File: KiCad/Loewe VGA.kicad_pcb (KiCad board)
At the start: 2 copper layers, 54.5 x 33.2 mm, 29 parts, among them U1 74HCT86

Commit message: Add project title and link to PCB silkscreen.
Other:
- board text added: "Loewe TVs Q2500 VGA Module"
- board text added: "github.com/proboterror/Loewe_VGA_Module_Q2500"
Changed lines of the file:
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@@
 			(at 4.315 -2.58 -90)
 			(layer "F.SilkS")
+			(hide yes)
 			(effects
 				(font
@@
 			(unlocked yes)
 			(layer "B.SilkS")
+			(hide yes)
 			(effects
 				(font
@@
 		)
 	)
+	(gr_text "github.com/proboterror/Loewe_VGA_Module_Q2500"
+		(at 172.307074 98.5 0)
+		(layer "B.SilkS")
+		(effects
+			(font
+				(size 1 1)
+				(thickness 0.15)
+			)
+			(justify left bottom mirror)
+		)
+	)
 	(gr_text "VCC"
 		(at 131.5 94.3 0)
@@
 			)
 			(justify left bottom mirror)
+		)
+	)
+	(gr_text "Loewe TVs Q2500 VGA Module"
+		(at 170.1 96.750072 0)
+		(layer "B.SilkS")
+		(effects
+			(font
+				(size 1.5 1.5)
+				(thickness 0.2)
+			)
+			(justify left bottom mirror)

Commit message: Connect VGA pin 8 to GND.
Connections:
- W801 pad 8: unconnected-(W801-Pad8) -> GND
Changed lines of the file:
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@@
 	(net 25 "unconnected-(W801-Pad0)")
 	(net 26 "unconnected-(W801-Pad0)_0")
-	(net 27 "unconnected-(W801-Pad8)")
-	(net 28 "unconnected-(W801-Pad4)")
-	(net 29 "unconnected-(W801-Pad9)")
+	(net 27 "unconnected-(W801-Pad4)")
+	(net 28 "unconnected-(W801-Pad9)")
 	(footprint "Capacitor_SMD:C_0805_2012Metric_Pad1.18x1.45mm_HandSolder"
 		(layer "F.Cu")
@@
 			(layers "*.Cu" "*.Mask")
 			(remove_unused_layers no)
-			(net 28 "unconnected-(W801-Pad4)")
+			(net 27 "unconnected-(W801-Pad4)")
 			(pintype "passive+no_connect")
 		)
@@
 			(layers "*.Cu" "*.Mask")
 			(remove_unused_layers no)
-			(net 27 "unconnected-(W801-Pad8)")
-			(pintype "passive+no_connect")
+			(net 1 "GND")
+			(pintype "passive")
 		)
 		(pad "9" thru_hole circle
@@
 			(layers "*.Cu" "*.Mask")
 			(remove_unused_layers no)
-			(net 29 "unconnected-(W801-Pad9)")
+			(net 28 "unconnected-(W801-Pad9)")
 			(pintype "passive+no_connect")
 		)

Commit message: Replace custom 3225 footprint for L826, L816 with standard 1210(3225). Add 4.7uH value for L826, L816 to schematic (use value from Q2300 board).
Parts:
- L816, L826: value LL3225M -> 4u7; footprint Loewe VGA:L3225M -> Inductor_SMD:L_1210_3225Metric_Pad1.42x2.65mm_HandSolder

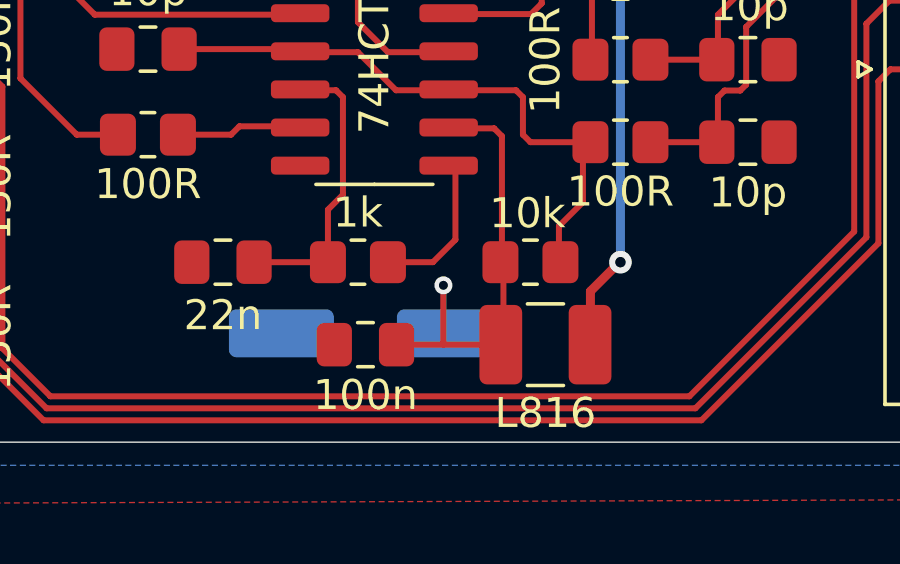
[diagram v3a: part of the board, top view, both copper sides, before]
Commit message: Add telegram channel link. Adjust power tracks width.
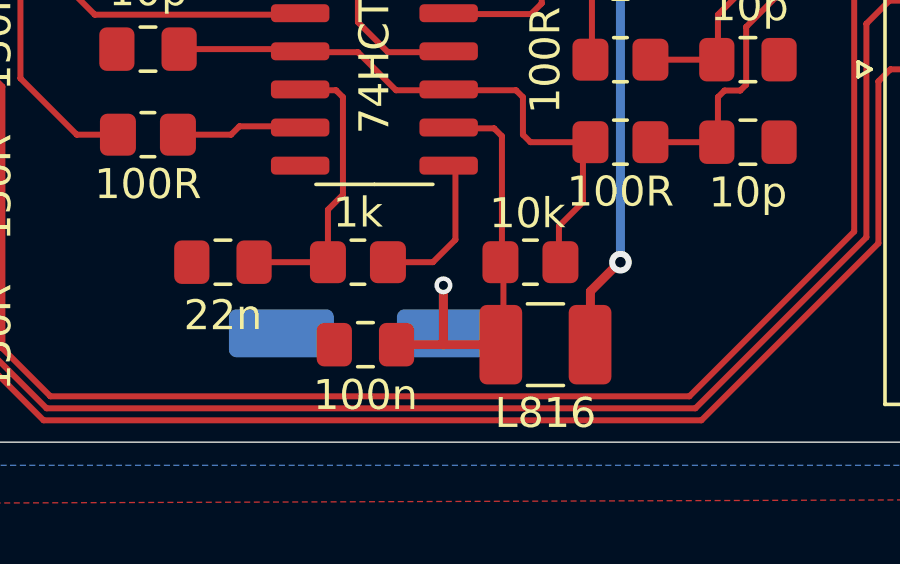
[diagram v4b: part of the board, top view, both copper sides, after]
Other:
- board text added: "github.com/proboterror/Loewe_VGA_Module_Q2500 t.me/dmg_crt"
- board text removed: "github.com/proboterror/Loewe_VGA_Module_Q2500"
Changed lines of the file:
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@@
 		)
 	)
-	(gr_text "github.com/proboterror/Loewe_VGA_Module_Q2500"
-		(at 172.307074 98.5 0)
-		(layer "B.SilkS")
-		(effects
-			(font
-				(size 1 1)
-				(thickness 0.15)
-			)
-			(justify left bottom mirror)
+	(gr_text "github.com/proboterror/Loewe_VGA_Module_Q2500\nt.me/dmg_crt"
+		(at 153.1 100.1 0)
+		(layer "B.SilkS")
+		(effects
+			(font
+				(size 1 1)
+				(thickness 0.15)
+			)
+			(justify bottom mirror)
 		)
 	)
@@
 		(start 147.1 118.3786)
 		(end 149.1011 118.3786)
-		(width 0.2)
+		(width 0.3)
 		(layer "F.Cu")
 		(net 5)
@@
 		(start 147.1 118.3786)
 		(end 147.1 116.4)
-		(width 0.2)
+		(width 0.3)
 		(layer "F.Cu")
 		(net 5)
@@
 		(start 145.5386 118.3786)
 		(end 147.1 118.3786)
-		(width 0.2)
+		(width 0.3)
 		(layer "F.Cu")
 		(net 5)
@@
 		(start 147.1 116.4)
 		(end 147.1 117.8)
-		(width 0.2)
+		(width 0.3)
 		(layer "B.Cu")
 		(net 5)

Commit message: Add R836~R838 RGB termination resistors note on PCB silkscreen.
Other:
- board text added: "Only for Q25 chassis"
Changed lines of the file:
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@@
+		)
+	)
+	(gr_text "Only for Q25 chassis"
+		(at 129.2 120.9 90)
+		(layer "F.SilkS")
+		(effects
+			(font
+				(size 1 1)
+				(thickness 0.15)
+			)
+			(justify left bottom)
 		)
 	)

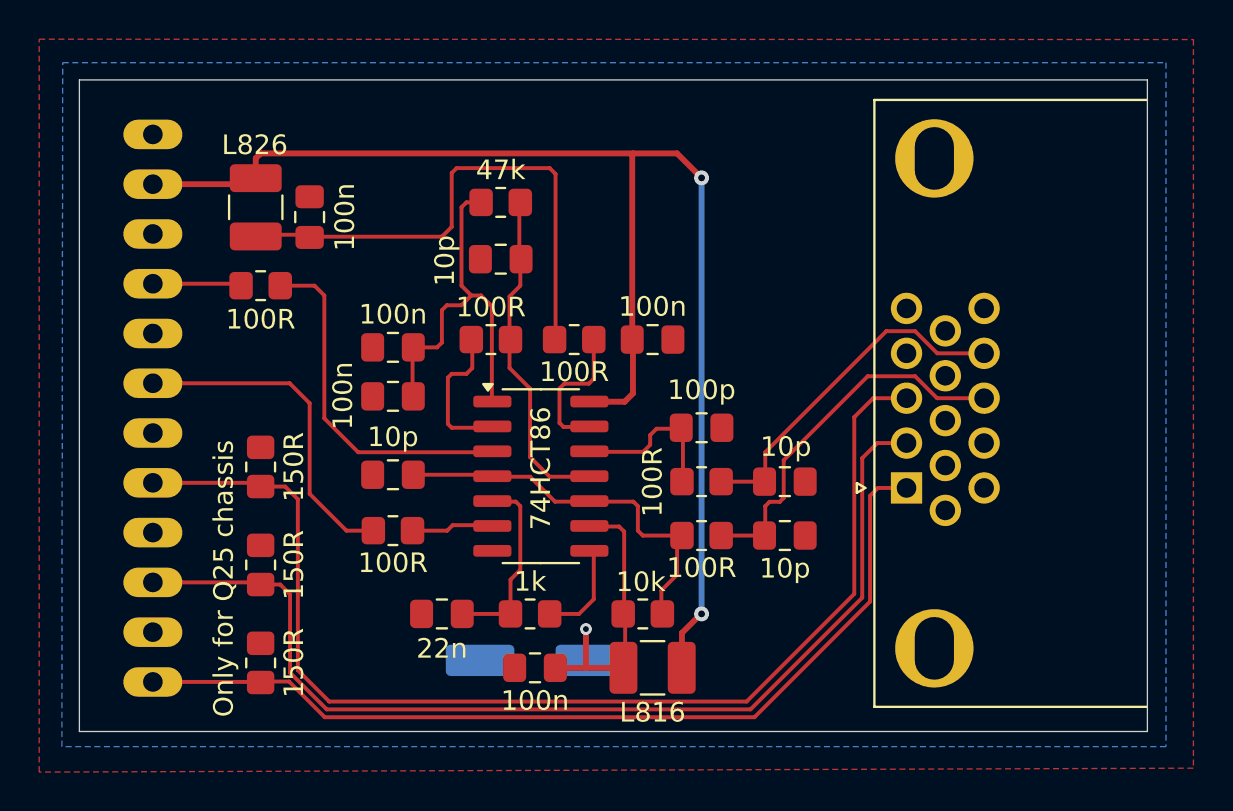
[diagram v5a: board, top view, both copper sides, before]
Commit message: Replace JST XH 2.50 mm with custom 2.54 mm. Remove unused Molex 22-23-2121 footprint. Add version V.1.1 label to PCB silkscreen.
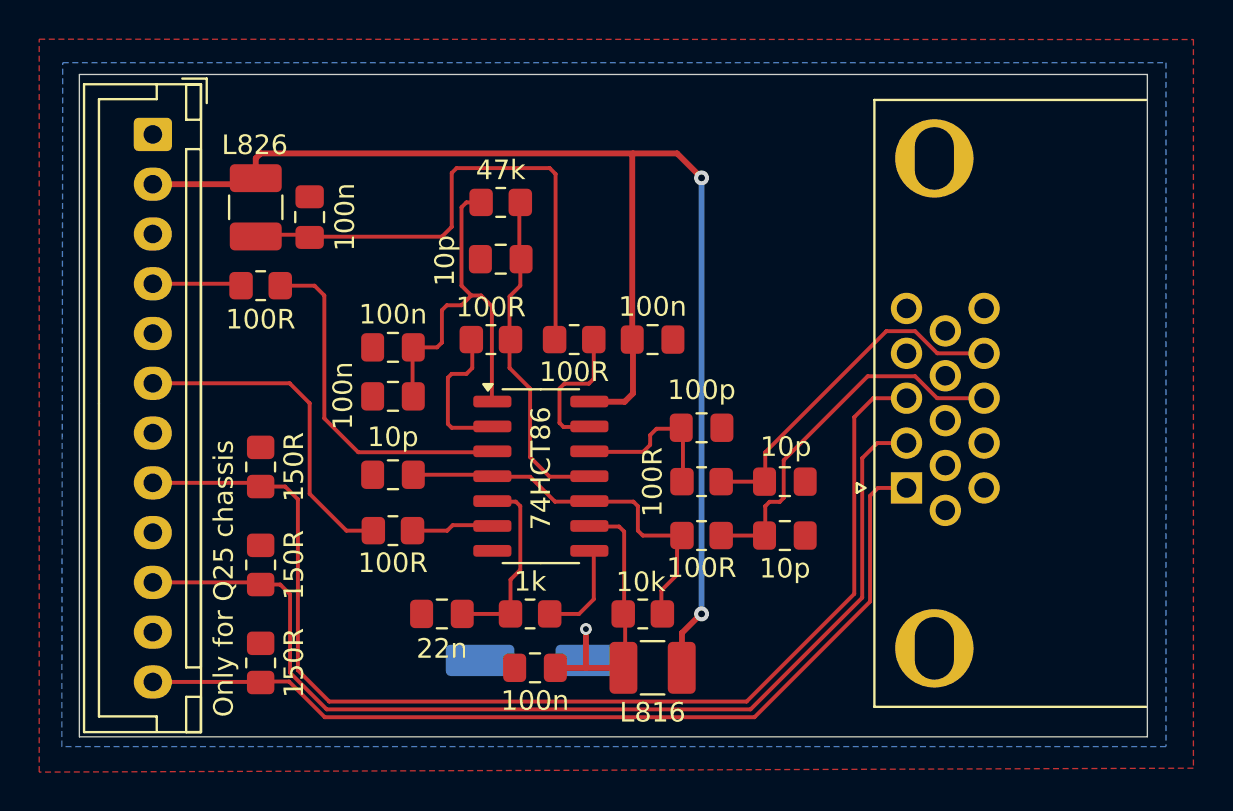
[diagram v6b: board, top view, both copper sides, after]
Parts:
- W831: value 22-23-2121 Molex -> TV; footprint Loewe VGA:22-23-2121 -> JST_XH_S10B_2.54mm:JST_XH_B12B-XH-A_1x12_P2.54mm_Vertical; moved to F.Cu
- moved W831 14.0 mm to (125.0, 91.2)
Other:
- board size 54.5 x 33.2 mm -> 54.5 x 33.8 mm
- board text added: "V.1.1"

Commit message: Replace incorrect Connector_Dsub:DSUB-15-HD_Male with short Connector_Dsub:DSUB-15-HD_Female. Move VGA and TV connectors to back side. Reduce PCB width. Change VCC tracks width from 0.3 to 0.5 mm. Align board info text.
PCB version updated to 1.2.
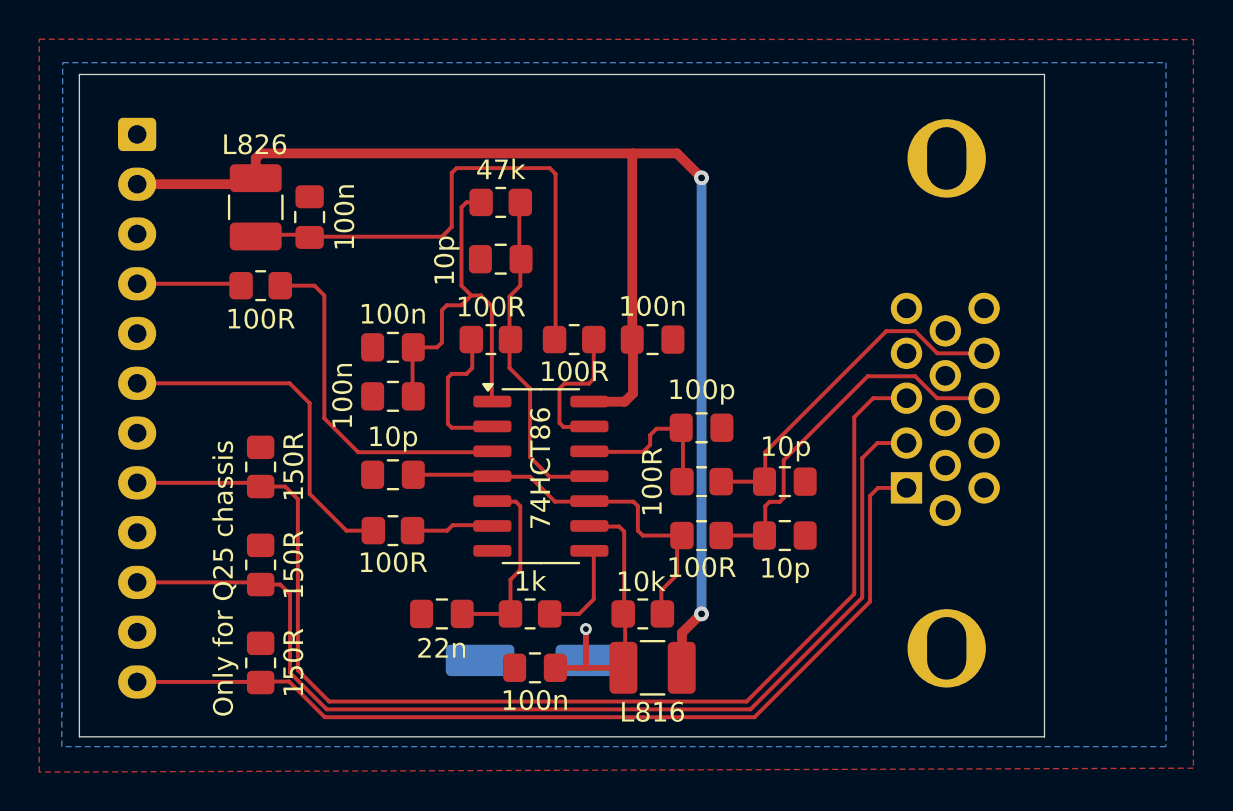
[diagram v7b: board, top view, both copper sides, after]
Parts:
- W801: footprint Connector_Dsub:DSUB-15-HD_Male_Horizontal_P2.29x1.98mm_EdgePinOffset8.35mm_Housed_MountingHolesOffset10.89mm -> Connector_Dsub:DSUB-15-HD_Female_Horizontal_P2.29x1.98mm_EdgePinOffset3.03mm_Housed_MountingHolesOffset4.94mm; moved to B.Cu
- W831: moved to B.Cu
- moved W831 0.80 mm to (124.2, 91.2)
- turned W801 to -90 degrees
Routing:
- net /GREEN: track 53.3 -> 54.1 mm
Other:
- board size 54.5 x 33.8 mm -> 49.2 x 33.8 mm
- board text added: "Loewe Q2500 VGA Module"
- board text added: "V.1.2"
- board text added: "github.com/proboterror/ Loewe_VGA_Module_Q2500 t.me/dmg_crt"
- board text removed: "Loewe TVs Q2500 VGA Module"
- board text removed: "V.1.1"
- board text removed: "github.com/proboterror/Loewe_VGA_Module_Q2500 t.me/dmg_crt"

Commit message: Add EDID EEPROM option for 848x480@60Hz mode auto detection with widescreen TVs.
PCB version 1.2.
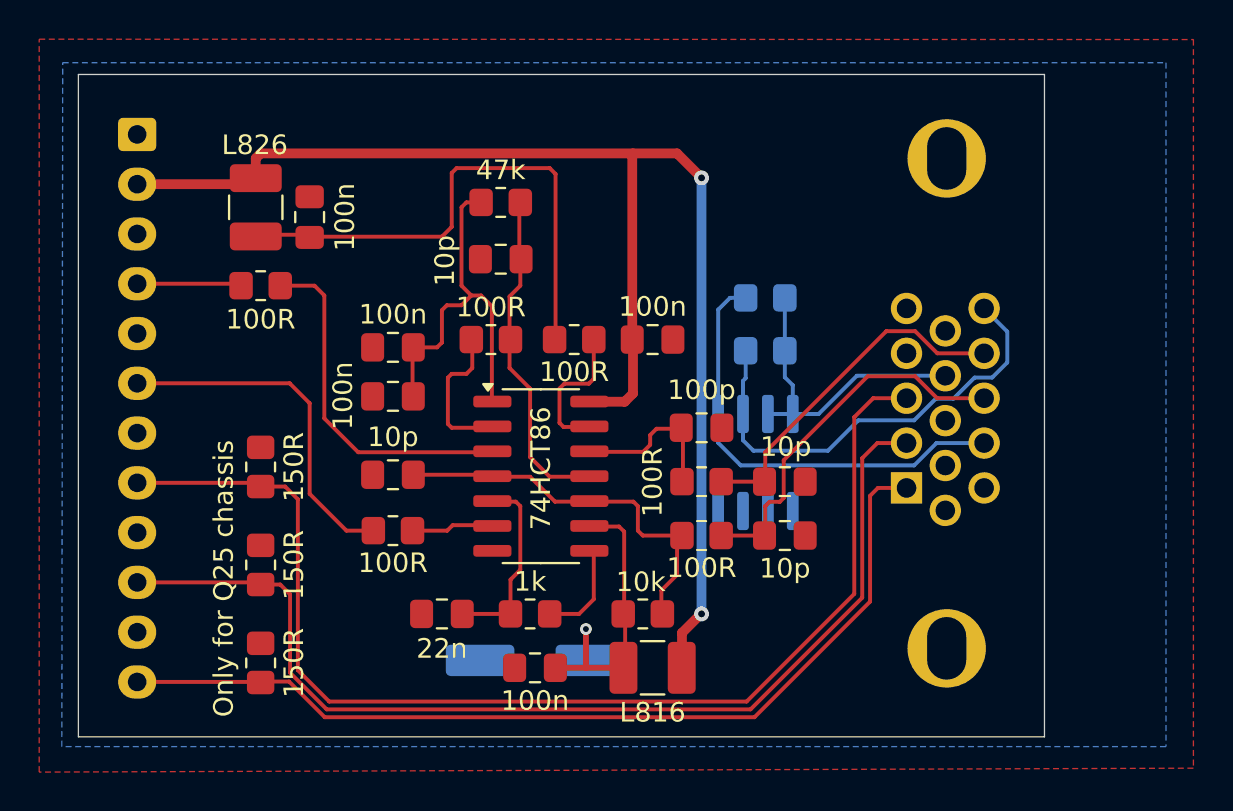
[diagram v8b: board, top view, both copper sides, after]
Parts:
- added R1: 2K2, Resistor_SMD:R_0805_2012Metric_Pad1.20x1.40mm_HandSolder, B.Cu at (156.2, 99.5)
- added R2: 2K2, Resistor_SMD:R_0805_2012Metric_Pad1.20x1.40mm_HandSolder, B.Cu at (156.2, 102.2)
- added U2: AT24C02, Package_SO:SOIC-8_3.9x4.9mm_P1.27mm, B.Cu at (155.8, 107.9)
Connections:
- W801 pad 12: unconnected-(W801-Pad12) -> /SDA
- W801 pad 15: unconnected-(W801-Pad15) -> /SCL
- W801 pad 9: unconnected-(W801-Pad9) -> /VGA_+5V
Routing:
- net /SCL: track 0.00 -> 23.4 mm
- net /SDA: track 0.00 -> 23.0 mm
- net /VGA_+5V: track 0.00 -> 16.0 mm
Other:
- board size 49.2 x 33.8 mm -> 49.3 x 33.8 mm
